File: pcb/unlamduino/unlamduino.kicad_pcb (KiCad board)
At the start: 2 copper layers, 38 parts, among them IC2 ATMEGA328-P, P3 CONN_01X08, U1 LM2576, U2 AP111733, Y2 16MHz

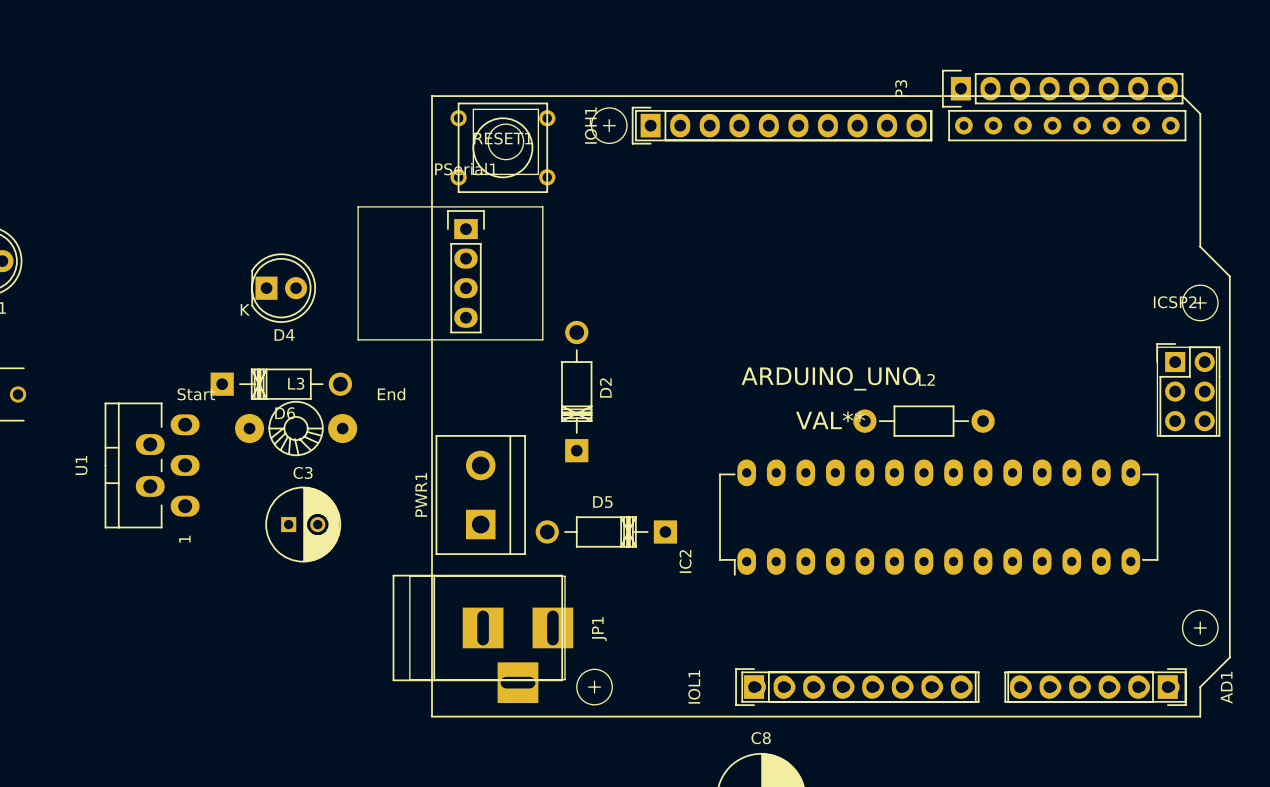
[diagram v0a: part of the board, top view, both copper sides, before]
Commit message: Colocacion en plantilla de conectores, alineados con grilla de 25, los que se pueden.
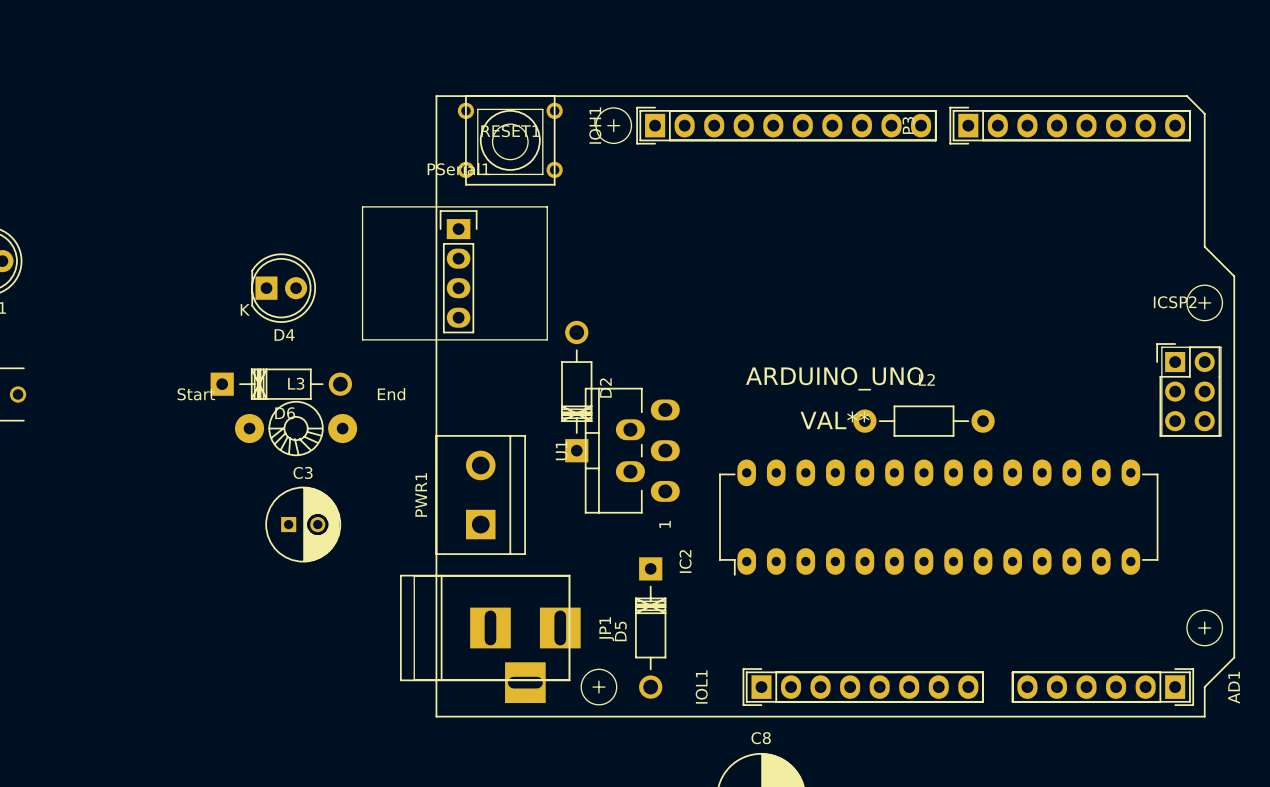
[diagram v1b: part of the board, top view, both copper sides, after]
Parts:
- moved U1 41.3 mm to (193.0, 80.6)
- moved D5 3.42 mm to (195.6, 90.8), turned to 270 degrees
- moved P3 3.24 mm to (222.9, 52.7)
- moved RESET1 0.90 mm to (183.5, 54.0)
- moved JP1 0.64 mm to (181.6, 95.9)
- moved PSerial1 0.64 mm to (179.1, 61.6)
- moved AD1 0.63 mm to (240.7, 101.0)
- moved IOL1 0.63 mm to (205.1, 101.0)
- moved ARDUINO_UNO 0.38 mm to (211.5, 76.8)
- moved IOH1 0.38 mm to (196.0, 52.7)
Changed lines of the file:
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@@
     (links 101)
     (no_connects 101)
-    (area 0 0 0 0)
+    (area 65.015 39.935 246.105 127.402001)
     (thickness 1.6)
     (drawings 0)
@@
   )
   (module Pin_Headers:Pin_Header_Straight_1x06 (layer F.Cu)
-    (at 240.03 100.965 270)
+    (at 240.665 100.965 270)
     (descr "Through hole pin header")
     (tags "pin header")
@@
   )
   (module Diodes_ThroughHole:Diode_DO-41_SOD81_Horizontal_RM10 (layer F.Cu)
-    (at 196.85 87.63 180)
+    (at 195.58 90.805 270)
     (descr "Diode, DO-41, SOD81, Horizontal, RM 10mm,")
     (tags "Diode, DO-41, SOD81, Horizontal, RM 10mm, 1N4007, SB140,")
-    (fp_text reference D5 (at 5.38734 2.53746 180) (layer F.SilkS)
-      (effects (font (size 1 1) (thickness 0.15)))
-    )
-    (fp_text value 1N4007 (at 4.37134 -3.55854 180) (layer F.Fab)
+    (fp_text reference D5 (at 5.38734 2.53746 270) (layer F.SilkS)
+      (effects (font (size 1 1) (thickness 0.15)))
+    )
+    (fp_text value 1N4007 (at 4.37134 -3.55854 270) (layer F.Fab)
       (effects (font (size 1 1) (thickness 0.15)))
     )
@@
     (fp_line (start 7.62 -1.27254) (end 7.62 1.26746) (layer F.SilkS) (width 0.15))
     (fp_line (start 7.62 1.26746) (end 2.54 1.26746) (layer F.SilkS) (width 0.15))
-    (pad 2 thru_hole circle (at 10.16 -0.00254) (size 1.99898 1.99898) (drill 1.27) (layers *.Cu *.Mask F.SilkS)
+    (pad 2 thru_hole circle (at 10.16 -0.00254 90) (size 1.99898 1.99898) (drill 1.27) (layers *.Cu *.Mask F.SilkS)
       (net 17 /VIN))
-    (pad 1 thru_hole rect (at 0 -0.00254) (size 1.99898 1.99898) (drill 1.00076) (layers *.Cu *.Mask F.SilkS)
+    (pad 1 thru_hole rect (at 0 -0.00254 90) (size 1.99898 1.99898) (drill 1.00076) (layers *.Cu *.Mask F.SilkS)
       (net 8 "Net-(C1-Pad1)"))
   )
@@
   )
   (module Pin_Headers:Pin_Header_Straight_1x10 (layer F.Cu)
-    (at 195.58 52.705 90)
+    (at 195.961 52.705 90)
     (descr "Through hole pin header")
     (tags "pin header")
@@
   )
   (module Pin_Headers:Pin_Header_Straight_1x08 (layer F.Cu)
-    (at 204.47 100.965 90)
+    (at 205.105 100.965 90)
     (descr "Through hole pin header")
     (tags "pin header")
@@
   )
   (module Connect:BARREL_JACK (layer F.Cu)
-    (at 180.975 95.885)
+    (at 181.61 95.885)
     (descr "DC Barrel Jack")
     (tags "Power Jack")
@@
   )
   (module Pin_Headers:Pin_Header_Straight_1x08 (layer F.Cu)
-    (at 222.25 49.53 90)
+    (at 222.885 52.705 90)
     (descr "Through hole pin header")
     (tags "pin header")
@@
   )
   (module Pin_Headers:Pin_Header_Straight_1x04 (layer F.Cu)
-    (at 179.705 61.595)
+    (at 179.07 61.595)
     (descr "Through hole pin header")
     (tags "pin header")
@@
   )
   (module Buttons_Switches_ThroughHole:SW_PUSH_SMALL (layer F.Cu)
-    (at 182.88 54.61)
+    (at 183.515 53.975)
     (fp_text reference RESET1 (at 0 -0.762) (layer F.SilkS)
       (effects (font (size 1 1) (thickness 0.15)))
@@
   )
   (module TO_SOT_Packages_THT:Pentawatt_Neutral_Staggered_Verical_TO220-5-T05D (layer F.Cu)
-    (at 151.765 81.915 90)
+    (at 193.04 80.645 90)
     (descr "Pentawatt, Neutral, Staggered, Verical, TO220-5, T05D,")
     (tags "Pentawatt, Neutral, Staggered, Verical, TO220-5, T05D,")
@@
   )
   (module SHIELD_ARDUINO:ARDUINO_as_UNO_R3_CONTOUR (layer F.Cu)
-    (at 211.074 76.835)
+    (at 211.455 76.835)
     (fp_text reference ARDUINO_UNO (at 0 -2.54) (layer F.SilkS)
       (effects (font (size 1.5 1.5) (thickness 0.15)))

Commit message: Acomodamiento preliminar de componentes, sin fuente 3v3
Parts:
- C10, C2, C4, C5, C6, C7, C9: footprint Capacitors_ThroughHole:C_Disc_D6_P5 -> Capacitors_ThroughHole:C_Disc_D3_P2.5
- D2, D5, D6: footprint Diodes_ThroughHole:Diode_DO-41_SOD81_Horizontal_RM10 -> Diodes_ThroughHole:Diode_DO-35_SOD27_Horizontal_RM10
- R1, R8, R9, RN1, RN2: footprint Resistors_ThroughHole:Resistor_Horizontal_RM15mm -> Resistors_ThroughHole:Resistor_Horizontal_RM7mm
- moved C20 140.3 mm to (221.5, 94.4)
- moved C21 140.3 mm to (226.3, 94.4)
- moved Y2 136.8 mm to (224.8, 95.9)
- moved R8 127.8 mm to (191.1, 63.5), turned to 180 degrees
- moved RN2 114.7 mm to (198.1, 57.1)
- moved R1 104.7 mm to (191.1, 73.7), turned to 270 degrees
- moved C7 101.2 mm to (227.3, 78.1)
- moved C10 100.1 mm to (219.1, 74.3)
- moved C5 90.2 mm to (198.1, 70.5)
- moved R9 86.3 mm to (191.1, 66.7), turned to 180 degrees
- moved RN1 83.7 mm to (189.9, 59.1), turned to 90 degrees
- moved C4 83.1 mm to (188.0, 87.0), turned to 90 degrees
- moved C9 76.1 mm to (203.8, 104.8)
- moved C1 72.4 mm to (195.6, 96.5), turned to 180 degrees
- moved C2 65.6 mm to (197.5, 101.0), turned to 180 degrees
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
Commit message: Añadido de agujeros M3 como en el Arduino original, ruteo preliminar con 10 puentes.
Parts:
- removed ARDUINO_UNO: VAL**, SHIELD_ARDUINO:ARDUINO_as_UNO_R3_CONTOUR
- added A1, A2, A3, A4: Agujero, Mounting_Holes:MountingHole_3.2mm_M3_DIN965_Pad, F.Cu at (0.00, 0.00)
- added REF**: MountingHole_3.2mm_M3, Mounting_Holes:MountingHole_3.2mm_M3, F.Cu at (192.4, 52.7)
- added REF**: MountingHole_3.2mm_M3, Mounting_Holes:MountingHole_3.2mm_M3, F.Cu at (243.2, 67.9)
- added REF**: MountingHole_3.2mm_M3, Mounting_Holes:MountingHole_3.2mm_M3, F.Cu at (243.2, 95.9)
- added REF**: MountingHole_3.2mm_M3, Mounting_Holes:MountingHole_3.2mm_M3, F.Cu at (191.1, 101.0)
- C8: footprint Capacitors_ThroughHole:C_Radial_D7.5_L11.2_P2.5 -> Capacitors_ThroughHole:C_Radial_D6.3_L11.2_P2.5
- moved RN1 62.5 mm to (248.3, 81.3), turned to 180 degrees
- moved IOL1 59.9 mm to (240.7, 52.7), turned to 270 degrees
- moved P3 51.4 mm to (205.1, 101.0)
- moved U2 49.0 mm to (188.0, 76.2), turned to 90 degrees
- moved IC2 34.8 mm to (237.5, 81.3), turned to 270 degrees
- moved D6 32.3 mm to (169.5, 88.9), turned to 90 degrees
- moved R1 29.0 mm to (162.6, 68.6), turned to 0 degrees
- moved C5 25.1 mm to (222.2, 77.5), turned to 180 degrees
- moved L2 24.9 mm to (216.5, 102.9), turned to 90 degrees
- moved L3 24.1 mm to (174.0, 85.1), turned to 90 degrees
- moved C21 22.9 mm to (216.5, 73.7)
- moved C20 22.0 mm to (221.6, 72.4), turned to 90 degrees
- moved Y2 21.9 mm to (221.0, 74.3), turned to 180 degrees
- moved C7 21.0 mm to (218.4, 97.2)
- moved R9 20.3 mm to (175.3, 54.0)
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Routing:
- net GND: track 0.00 -> 362.7 mm, vias 0 -> 2
- net +5V: track 0.00 -> 346.6 mm, vias 0 -> 7
- net /RESET: track 0.00 -> 253.6 mm, vias 0 -> 4
- net /IO13: track 0.00 -> 155.2 mm
- net /AD4/SDA: track 0.00 -> 140.6 mm, vias 0 -> 2
- net /IO12: track 0.00 -> 129.5 mm
- net /IO0: track 0.00 -> 123.2 mm
- net /AD5/SCL: track 0.00 -> 118.3 mm, vias 0 -> 2
- net /IO1: track 0.00 -> 110.3 mm
- net /IO11: track 0.00 -> 102.6 mm
- net /VIN: track 0.00 -> 96.9 mm
- net +3V3: track 0.00 -> 56.8 mm
- net /IO10: track 0.00 -> 50.3 mm
- net /IO9: track 0.00 -> 43.2 mm
- net /IO7: track 0.00 -> 38.5 mm
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
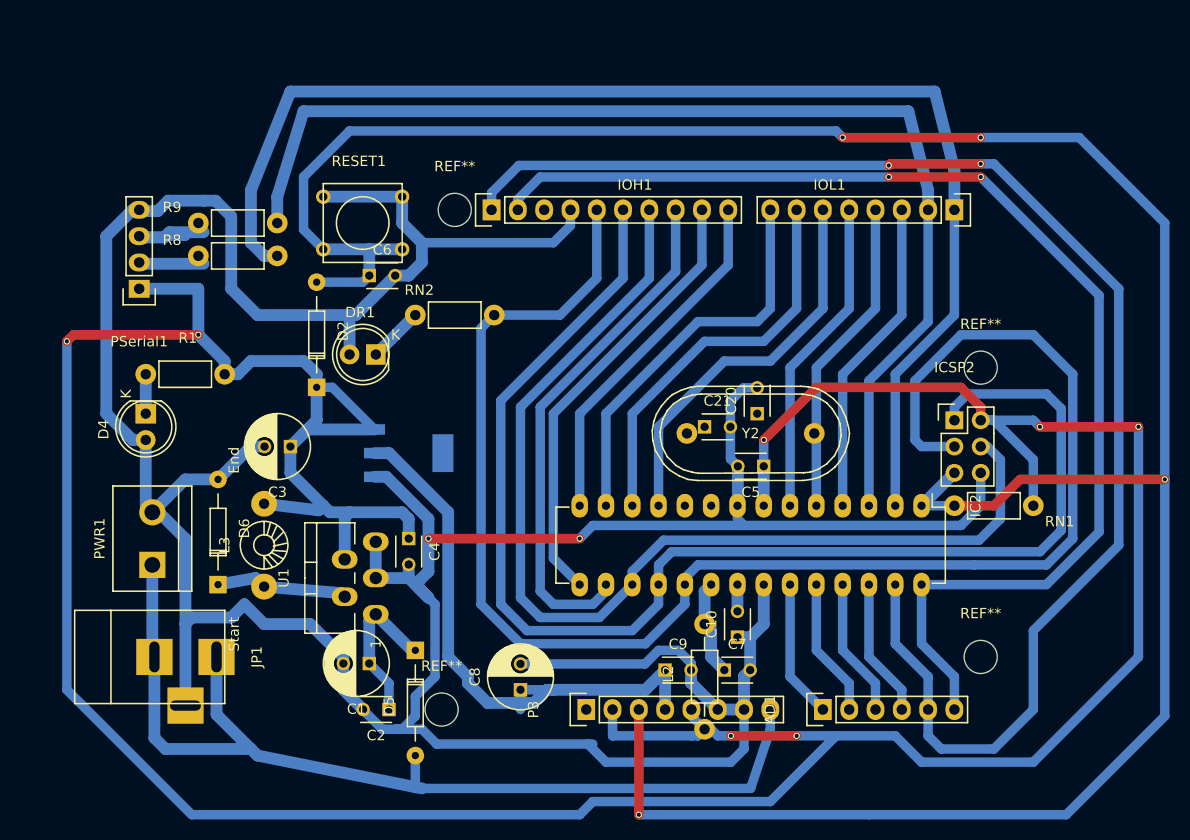
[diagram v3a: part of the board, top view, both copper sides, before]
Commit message: Ruteo en 0,6mm de pista para hacer una aproximación al definitivo.
Eliminación del puente de reset. Reacomodamiento de resistor de reset.
Ver capa de reset que quedó en el pulsador.
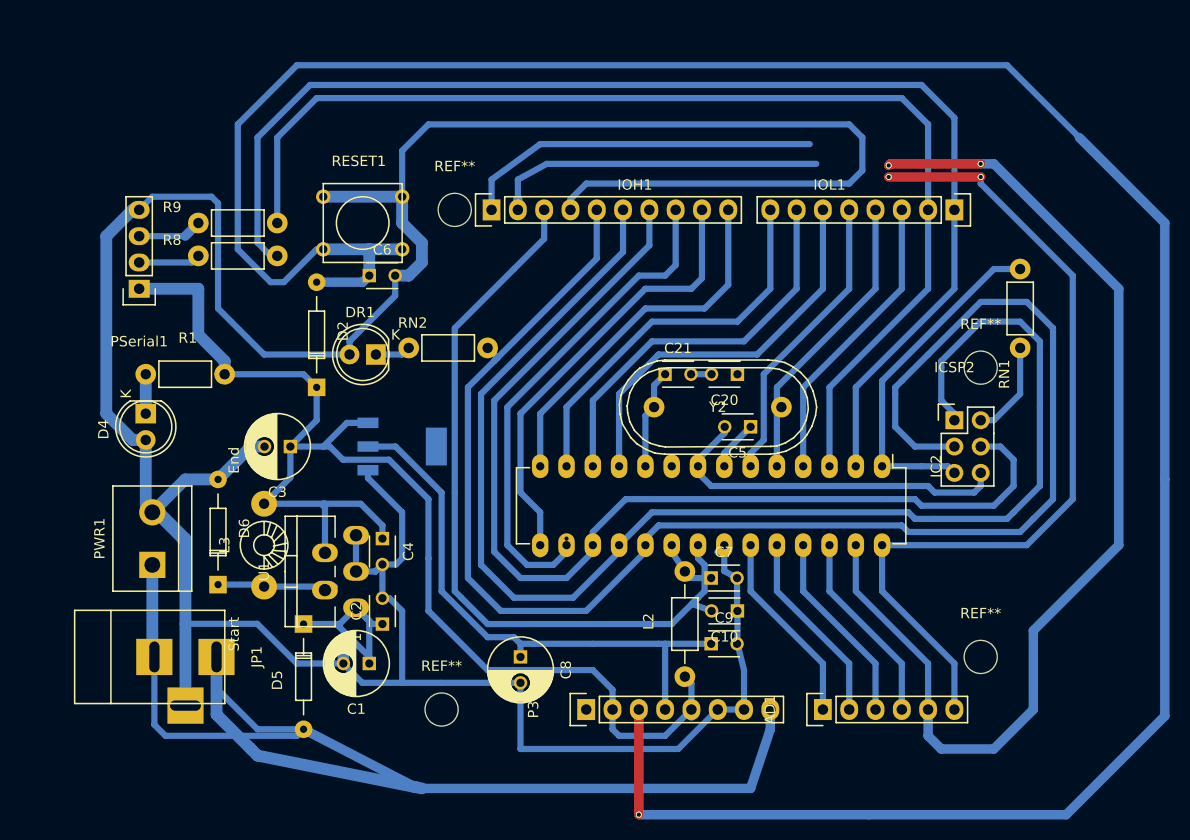
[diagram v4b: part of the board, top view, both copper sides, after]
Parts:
- moved RN1 15.3 mm to (247.0, 66.0), turned to 90 degrees
- moved D5 11.1 mm to (177.8, 92.7)
- moved C7 8.98 mm to (217.2, 88.3)
- moved C2 8.28 mm to (185.4, 92.7), turned to 90 degrees
- moved C21 6.35 mm to (212.7, 68.6)
- moved L2 5.43 mm to (214.6, 97.8)
- moved IC2 5.39 mm to (233.7, 77.5)
- moved C9 5.12 mm to (217.2, 94.6)
- moved C20 4.26 mm to (219.7, 68.6), turned to 180 degrees
- moved Y2 4.07 mm to (217.8, 71.8)
- moved C5 4.02 mm to (221.0, 73.7)
- moved RN2 3.24 mm to (188.0, 66.0)
- moved C8 3.17 mm to (198.8, 95.9), turned to 270 degrees
- moved C4 2.54 mm to (185.4, 84.5)
- moved C10 2.54 mm to (219.7, 91.4), turned to 180 degrees
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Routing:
- net +5V: track 346.6 -> 140.0 mm, vias 7 -> 0
- net /AREF: track 2.58 -> 74.7 mm
- net /RESET: track 253.6 -> 282.5 mm, vias 4 -> 1
- net /VIN: track 96.9 -> 123.2 mm
- net GND: track 362.7 -> 384.5 mm, vias 2 -> 0
- net /XTAL2: track 0.00 -> 9.68 mm
- net Net-(C1-Pad1): track 15.5 -> 23.1 mm
- net /AD2: track 13.4 -> 18.8 mm
- net /AD1: track 13.4 -> 18.8 mm
- net /AD3: track 13.4 -> 18.8 mm
- net /AD0: track 13.4 -> 18.8 mm
- net Net-(PSerial1-Pad3): track 12.5 -> 8.04 mm
- net Net-(C7-Pad1): track 9.31 -> 5.73 mm
- net /IO12: track 129.5 -> 132.7 mm
- net +3V3: track 56.8 -> 54.2 mm
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
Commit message: Acomodado de componentes para mejorar ruteo, minimización de pistas faltantes.
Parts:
- removed A1, A2, A3, A4: Agujero, Mounting_Holes:MountingHole_3.2mm_M3_DIN965_Pad
- moved D2 14.6 mm to (167.0, 61.6), turned to 0 degrees
- moved C8 11.7 mm to (191.1, 87.0), turned to 180 degrees
- moved C4 6.87 mm to (179.7, 80.6), turned to 0 degrees
- moved R1 5.99 mm to (167.6, 65.4)
- moved C3 5.39 mm to (172.7, 71.8)
- moved DR1 5.12 mm to (179.7, 67.3), turned to 0 degrees
- moved C2 4.84 mm to (181.0, 94.6), turned to 0 degrees
- moved D5 3.81 mm to (174.0, 92.7)
- moved L2 3.81 mm to (210.8, 97.8)
- moved C1 3.24 mm to (183.5, 99.7)
- moved D4 2.62 mm to (161.9, 69.8), turned to 0 degrees
- moved C10 2.54 mm to (217.2, 91.4)
- moved RN1 2.54 mm to (247.0, 63.5)
- moved C7 2.54 mm to (214.6, 88.3)
- moved C9 2.54 mm to (214.6, 94.6)
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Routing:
- net +5V: track 140.0 -> 297.5 mm, vias 0 -> 4
- net GND: track 384.5 -> 526.4 mm, vias 0 -> 2
- net /VIN: track 123.2 -> 91.6 mm
- net /RESET: track 282.5 -> 266.5 mm, vias 1 -> 4
- net /AD5/SCL: track 115.9 -> 128.6 mm
- net /AD4/SDA: track 139.7 -> 148.2 mm
- net Net-(DR1-Pad1): track 3.44 -> 11.6 mm
- net Net-(D4-Pad1): track 3.81 -> 9.42 mm
- net /IO7: track 37.8 -> 33.3 mm
- net /IO6: track 38.1 -> 33.7 mm
- net /IO5: track 38.5 -> 34.0 mm
- net /IO8: track 35.6 -> 32.3 mm
- net /IO13: track 152.6 -> 155.8 mm
- net /IO12: track 132.7 -> 135.8 mm
- net Net-(C7-Pad1): track 5.73 -> 8.41 mm
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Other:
- net class Default: via_dia 0.6 -> 2.5; via_drill 0.4 -> 0.8
